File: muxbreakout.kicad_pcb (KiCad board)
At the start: 2 copper layers, 23.4 x 25.4 mm, 3 parts, among them J1 1x10_pins_L, J2 1x10_pins_R, U1 mux

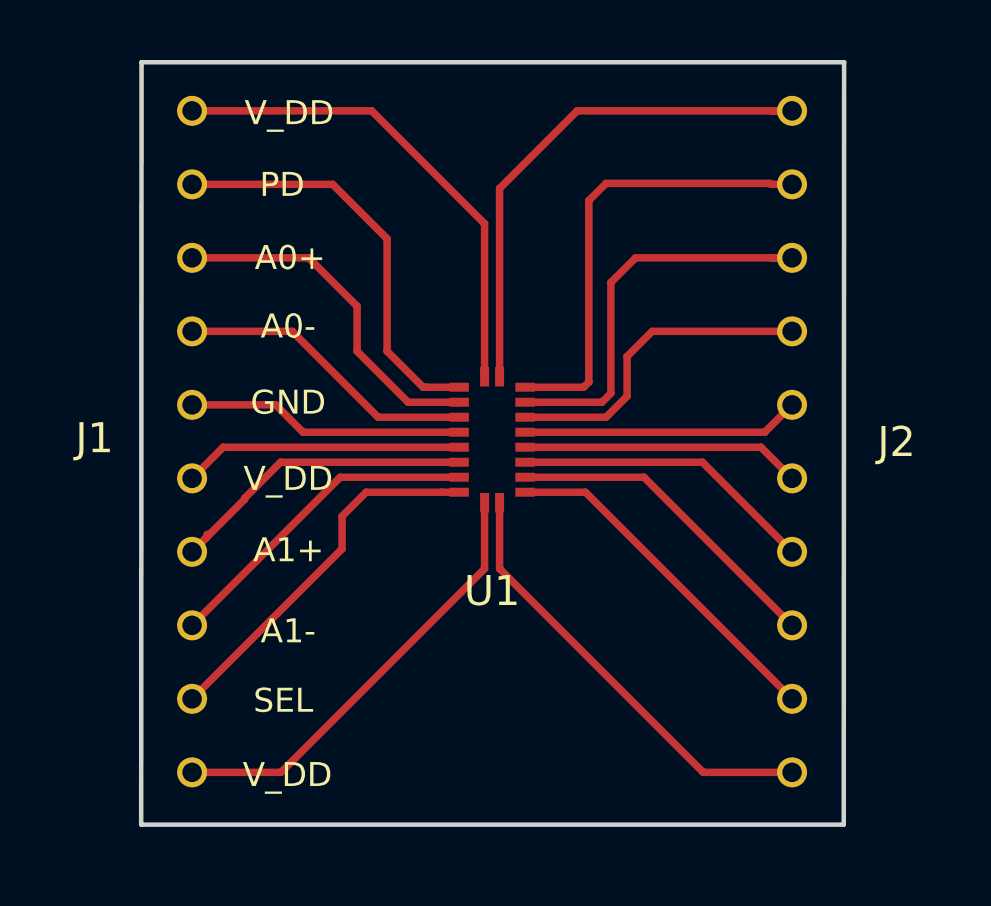
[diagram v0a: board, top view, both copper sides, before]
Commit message: pcb edge fixed
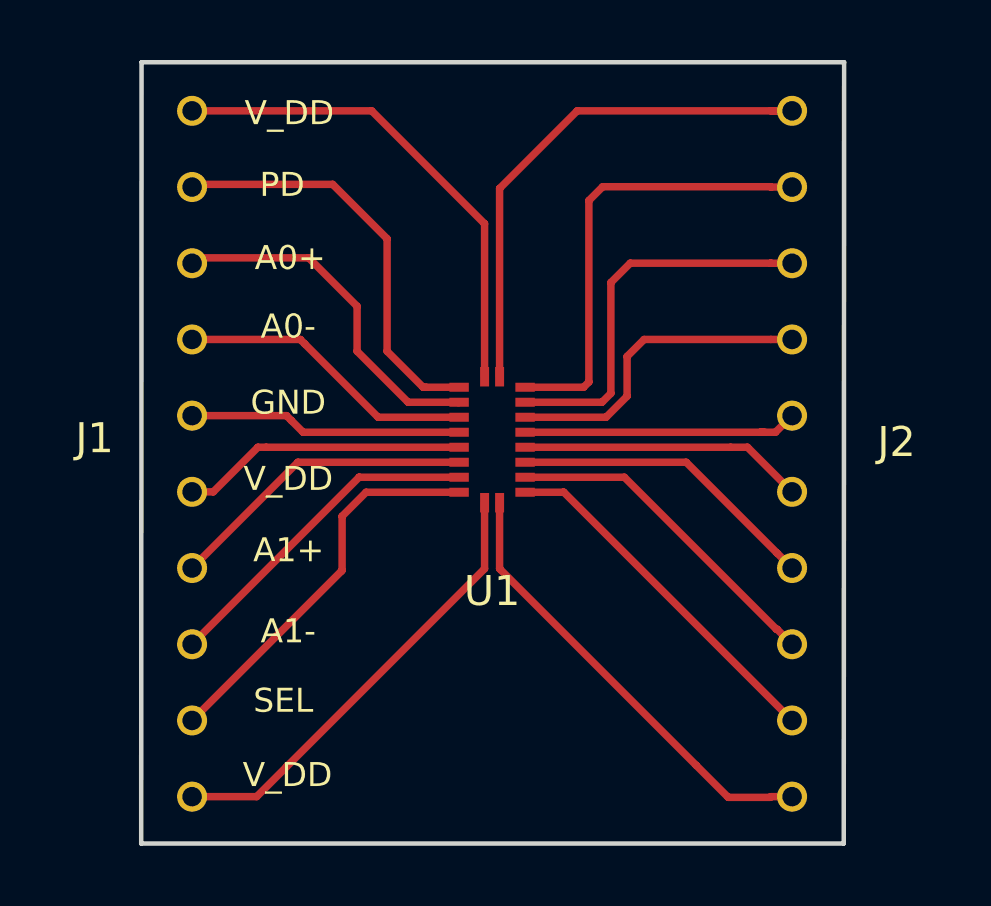
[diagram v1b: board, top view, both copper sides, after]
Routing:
- net Net-(J2-Pad3): track 13.8 -> 13.0 mm
- net Net-(J1-Pad9): track 12.4 -> 13.1 mm
- net Net-(J1-Pad7): track 11.0 -> 10.4 mm
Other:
- board size 23.4 x 25.4 mm -> 23.4 x 26 mm
